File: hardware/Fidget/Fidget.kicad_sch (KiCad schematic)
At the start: 41 parts

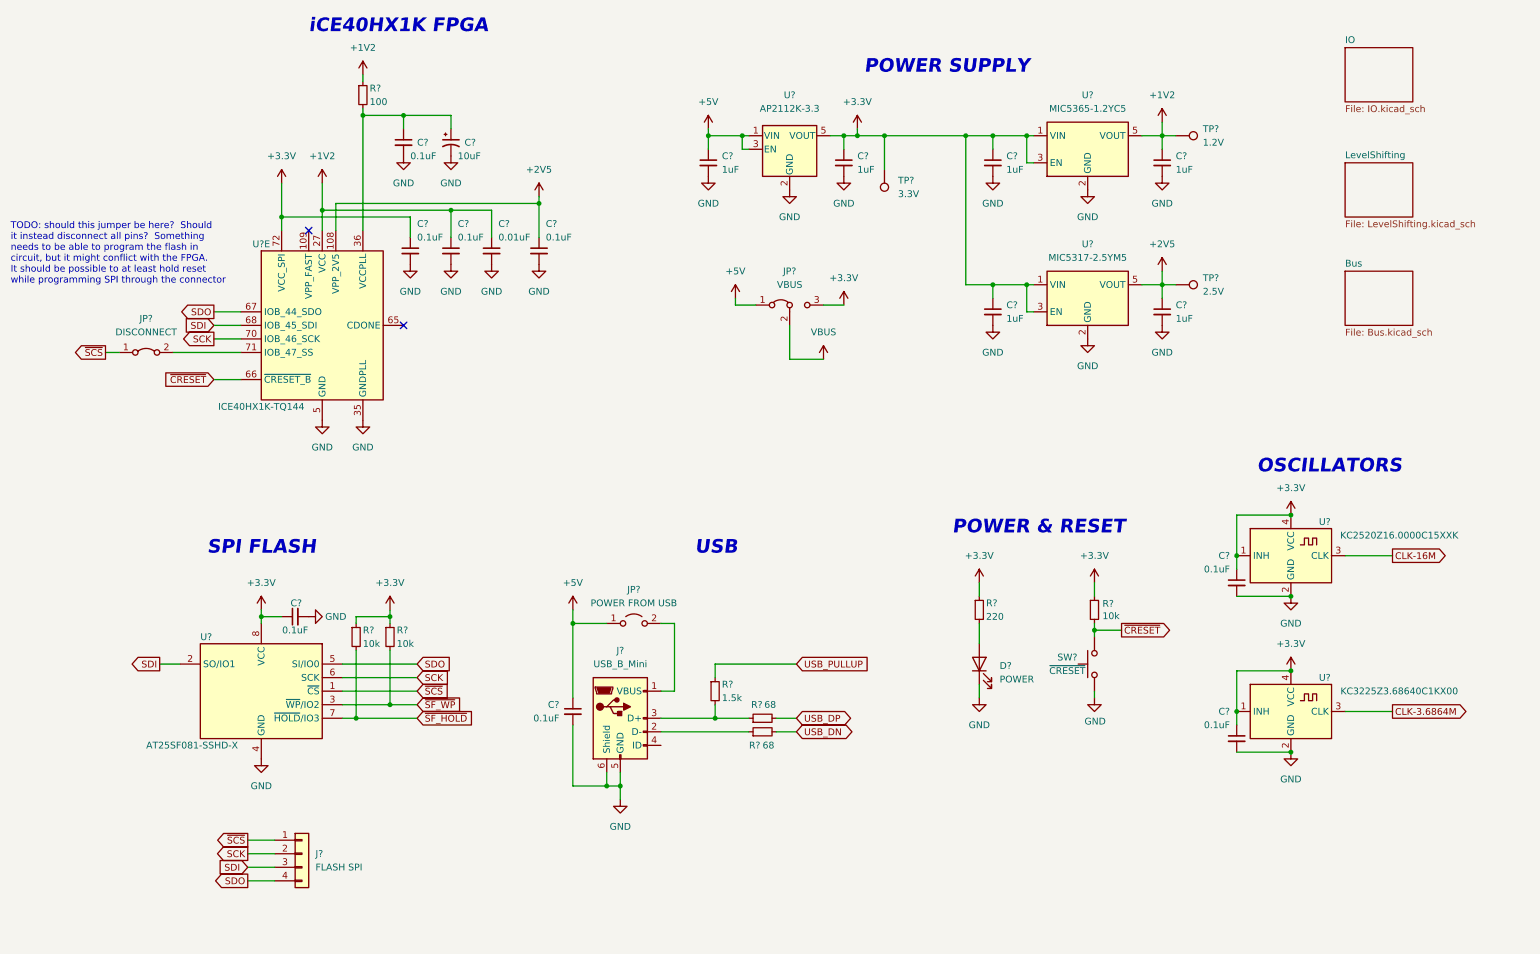
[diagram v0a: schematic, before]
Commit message: Minor updates, and start of PCB layout
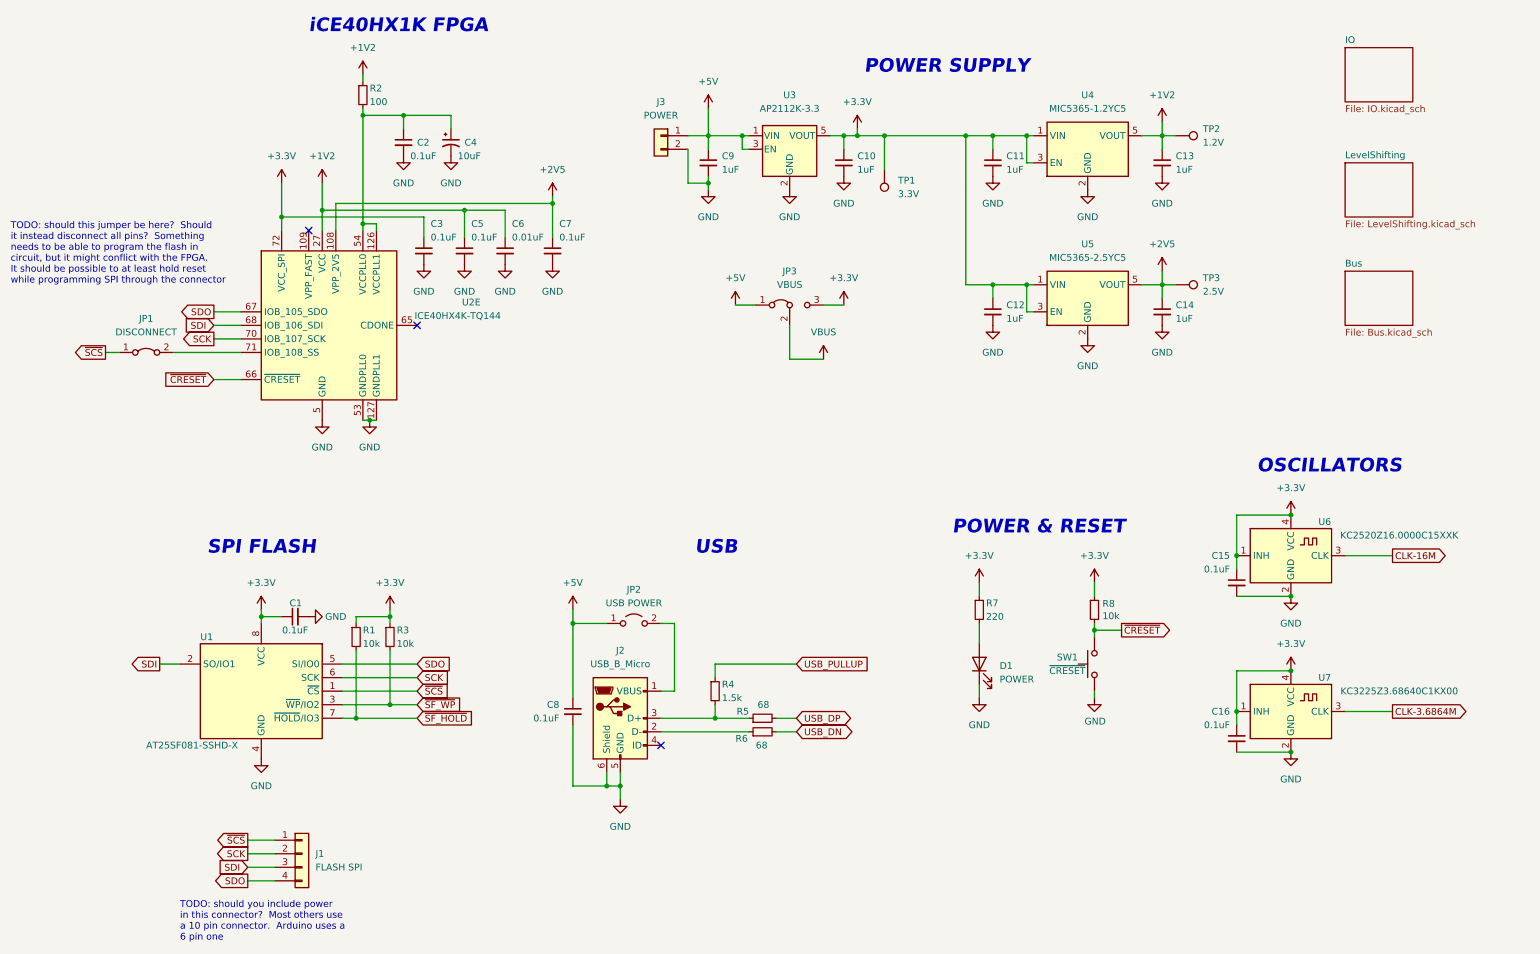
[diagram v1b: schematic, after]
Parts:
- removed U?: ICE40HX1K-TQ144, Package_QFP:TQFP-144_20x20mm_P0.5mm, symbol FPGA_Lattice:ICE40HX1K-TQ144
- added J3: POWER, Connector_PinHeader_2.54mm:PinHeader_1x02_P2.54mm_Vertical, symbol Connector_Generic:Conn_01x02
- added U2: ICE40HX4K-TQ144, Package_QFP:TQFP-144_20x20mm_P0.5mm, symbol FPGA_Lattice:ICE40HX4K-TQ144
- C1, C15, C16, C2, C3, C5, C6, C7, C8: renamed from C?; footprint (none) -> Capacitor_SMD:C_0805_2012Metric_Pad1.18x1.45mm_HandSolder
- C10, C11, C12, C13, C14, C4, C9: renamed from C?; footprint (none) -> Capacitor_SMD:C_1206_3216Metric_Pad1.33x1.80mm_HandSolder
- J1: renamed from J?; footprint (none) -> Connector_PinHeader_2.54mm:PinHeader_1x04_P2.54mm_Vertical
- J2: renamed from J?; value USB_B_Mini -> USB_B_Micro; footprint (none) -> Connector_USB:USB_Micro-B_Amphenol_10118194_Horizontal; symbol Connector:USB_B_Mini -> Connector:USB_B_Micro
- JP1: renamed from JP?; footprint (none) -> Connector_PinHeader_2.54mm:PinHeader_1x02_P2.54mm_Vertical
- JP2: renamed from JP?; value POWER FROM USB -> USB POWER; footprint (none) -> Connector_PinHeader_2.54mm:PinHeader_1x02_P2.54mm_Vertical
- JP3: renamed from JP?; footprint (none) -> Connector_PinHeader_2.54mm:PinHeader_1x03_P2.54mm_Vertical
- R1, R2, R3, R4, R5, R6: renamed from R?; footprint (none) -> Resistor_SMD:R_0805_2012Metric_Pad1.20x1.40mm_HandSolder
- R7: renamed from R?; footprint (none) -> Resistor_THT:R_Axial_DIN0204_L3.6mm_D1.6mm_P5.08mm_Horizontal
- TP1, TP2, TP3: renamed from TP?; footprint (none) -> TestPoint:TestPoint_THTPad_2.0x2.0mm_Drill1.0mm
- U3: renamed from U?; footprint Package_TO_SOT_SMD:SOT-23-5 -> Package_TO_SOT_SMD:SOT-23-5_HandSoldering
- U4: renamed from U?; footprint Package_TO_SOT_SMD:SOT-353_SC-70-5 -> Package_TO_SOT_SMD:SOT-353_SC-70-5_Handsoldering
- U5: renamed from U?; value MIC5317-2.5YM5 -> MIC5365-2.5YC5; footprint Package_TO_SOT_SMD:SOT-23-5_HandSoldering -> Package_TO_SOT_SMD:SOT-353_SC-70-5_Handsoldering
- gave numbers to parts that had none: 6
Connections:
- net +1V2: now also U2.111 (VCC), U2.27 (VCC), U2.40 (VCC), U2.92 (VCC)
- net +2V5: now also U2.108 (VPP_2V5)
- net +3.3V: now also U2.72 (VCC_SPI)
- net +5V: now also J3.1 (Pin_1)
- net GND: now also J3.2 (Pin_2), U2.103 (GND), U2.127 (GNDPLL1), U2.13 (GND), U2.132 (GND), U2.14 (GND), U2.140 (GND), U2.5 (GND), U2.53 (GNDPLL0), U2.59 (GND), U2.69 (GND), U2.86 (GND)
- net SCK: now also U2.70 (IOB_107_SCK)
- net SDI: now also U2.68 (IOB_106_SDI)
- net SDO: now also U2.67 (IOB_105_SDO)
- net ~{CRESET}: now also U2.66 (~{CRESET})
- net at JP1.2 (B): now also U2.71 (IOB_108_SS)
- net at C2.1, C4.1, R2.2: now also U2.126 (VCCPLL1), U2.54 (VCCPLL0)
- no-connect marks 2 -> 3
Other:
- note added: "TODO: should you include power in this connector? Most others use a 10 pin connector. Arduino uses a 6 pin one"
- moved on the sheet: C3, C5, C6, C7

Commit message: More PCB layout and fixes and reassigments to the schematics
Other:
- note added: "iCE40HX4K FPGA"
- note removed: "iCE40HX1K FPGA"
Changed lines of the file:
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@@
     (effects (font (size 2.56 2.56) (thickness 0.254) bold italic) (justify left bottom))
   )
-  (text "iCE40HX1K FPGA" (at 60.96 20.32 0)
+  (text "iCE40HX4K FPGA" (at 60.96 20.32 0)
     (effects (font (size 2.56 2.56) (thickness 0.254) bold italic) (justify left bottom))
   )
@@
       (reference "#PWR0120") (unit 1) (value "+5V") (footprint "")
     )
-    (path "/f7dd7bf3-1de8-4cd8-8394-417b8f446de5/bfca4ce6-4fe2-4800-9300-c9e736fe9712"
-      (reference "#PWR0121") (unit 1) (value "+5V") (footprint "")
-    )
-    (path "/f7dd7bf3-1de8-4cd8-8394-417b8f446de5/d29ac653-05fc-43a6-bc92-097a1022dd41"
-      (reference "#PWR0122") (unit 1) (value "+5V") (footprint "")
-    )
     (path "/f7dd7bf3-1de8-4cd8-8394-417b8f446de5/1d36a57b-949f-4615-b91a-64bfc14f44ee"
       (reference "#PWR0123") (unit 1) (value "+5V") (footprint "")
@@
       (reference "#PWR0124") (unit 1) (value "+5V") (footprint "")
     )
+    (path "/f7dd7bf3-1de8-4cd8-8394-417b8f446de5/104af919-8d5f-494d-9f35-62418a6a067e"
+      (reference "#PWR?") (unit 1) (value "VBUS") (footprint "")
+    )
+    (path "/f7dd7bf3-1de8-4cd8-8394-417b8f446de5/fcbc81d8-8649-4a2c-8522-174e40417a6b"
+      (reference "#PWR?") (unit 1) (value "VBUS") (footprint "")
+    )
     (path "/c6cb8ea6-4882-46c7-9da7-5c05514eceac"

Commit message: Almost done Rev1 board design
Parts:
- removed JP1: DISCONNECT, Connector_PinHeader_2.54mm:PinHeader_1x02_P2.54mm_Vertical, symbol Jumper:Jumper_2_Bridged
- D1: footprint (none) -> LED_SMD:LED_PLCC-2_3.4x3.0mm_KA
- J1: footprint Connector_PinHeader_2.54mm:PinHeader_1x04_P2.54mm_Vertical -> Connector_PinHeader_2.54mm:PinHeader_2x04_P2.54mm_Vertical; symbol Connector_Generic:Conn_01x04 -> Connector_Generic:Conn_02x04_Odd_Even
- J3: value POWER -> +5Vin
- R7, R8: footprint Resistor_THT:R_Axial_DIN0204_L3.6mm_D1.6mm_P5.08mm_Horizontal -> Resistor_SMD:R_0805_2012Metric_Pad1.20x1.40mm_HandSolder
- U1: value AT25SF081-SSHD-X -> AT25SF081-SSHD
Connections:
- net +3.3V: now also J1.1 (Pin_1)
- net GND: now also J1.2 (Pin_2)
- net SCK: now also J1.5 (Pin_5); no longer J1.2 (Pin_2)
- net SDI: now also J1.8 (Pin_8); no longer J1.3 (Pin_3)
- net SDO: now also J1.7 (Pin_7); no longer J1.4 (Pin_4)
- net ~{SCS}: now also J1.6 (Pin_6), U2.71 (IOB_108_SS); no longer J1.1 (Pin_1)
- net ~{SF_HOLD}: now also J1.3 (Pin_3)
- net ~{SF_WP}: now also J1.4 (Pin_4)
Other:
- note removed: "TODO: should this jumper be here? Should it instead disconnect all pins? Something needs to be able to program the flash in circuit, but it might conflict with the FPGA. It should be possible to at least hold reset while programming SPI through the connector"
- note removed: "TODO: should you include power in this connector? Most others use a 10 pin connector. Arduino uses a 6 pin one"

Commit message: Changed crystal footprint and minor cleanup of Rev1 PCB
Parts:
- U7: footprint Oscillator:Oscillator_SMD_Kyocera_KC2520Z-4Pin_2.5x2.0mm -> Crystal:Crystal_SMD_3225-4Pin_3.2x2.5mm_HandSoldering
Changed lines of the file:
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@@
     (property "Reference" "U7" (id 0) (at 251.46 140.97 0))
     (property "Value" "KC3225Z3.68640C1KX00" (id 1) (at 265.43 143.51 0))
-    (property "Footprint" "Oscillator:Oscillator_SMD_Kyocera_KC2520Z-4Pin_2.5x2.0mm" (id 2) (at 248.92 143.51 0)
+    (property "Footprint" "Crystal:Crystal_SMD_3225-4Pin_3.2x2.5mm_HandSoldering" (id 2) (at 248.92 143.51 0)
       (effects (font (size 1.27 1.27)) hide)
     )
@@
     )
     (path "/940bf462-1fcf-41ca-8f3e-0e1903d6f959"
-      (reference "U7") (unit 1) (value "KC3225Z3.68640C1KX00") (footprint "Oscillator:Oscillator_SMD_Kyocera_KC2520Z-4Pin_2.5x2.0mm")
+      (reference "U7") (unit 1) (value "KC3225Z3.68640C1KX00") (footprint "Crystal:Crystal_SMD_3225-4Pin_3.2x2.5mm_HandSoldering")
     )
     (path "/636ee855-2082-46e2-a822-b2da99283a14/5201c52f-b863-460e-901b-433e53f09b6a"
